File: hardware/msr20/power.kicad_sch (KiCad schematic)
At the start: 6 parts, among them U8 NCP1117-3.3_SOT223, U9 NCP1117-5.0_SOT223

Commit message: update footprint assignments for passives
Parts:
- C10, C11, C12, C13: footprint (none) -> Capacitor_SMD:C_0805_2012Metric
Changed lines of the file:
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@@
 			)
 		)
-		(property "Footprint" ""
+		(property "Footprint" "Capacitor_SMD:C_0805_2012Metric"
 			(at 152.0952 86.36 0)
 			(effects
@@
 			)
 		)
-		(property "Footprint" ""
+		(property "Footprint" "Capacitor_SMD:C_0805_2012Metric"
 			(at 181.3052 86.36 0)
 			(effects
@@
 			)
 		)
-		(property "Footprint" ""
+		(property "Footprint" "Capacitor_SMD:C_0805_2012Metric"
 			(at 105.1052 86.36 0)
 			(effects
@@
 			)
 		)
-		(property "Footprint" ""
+		(property "Footprint" "Capacitor_SMD:C_0805_2012Metric"
 			(at 74.6252 86.36 0)
 			(effects

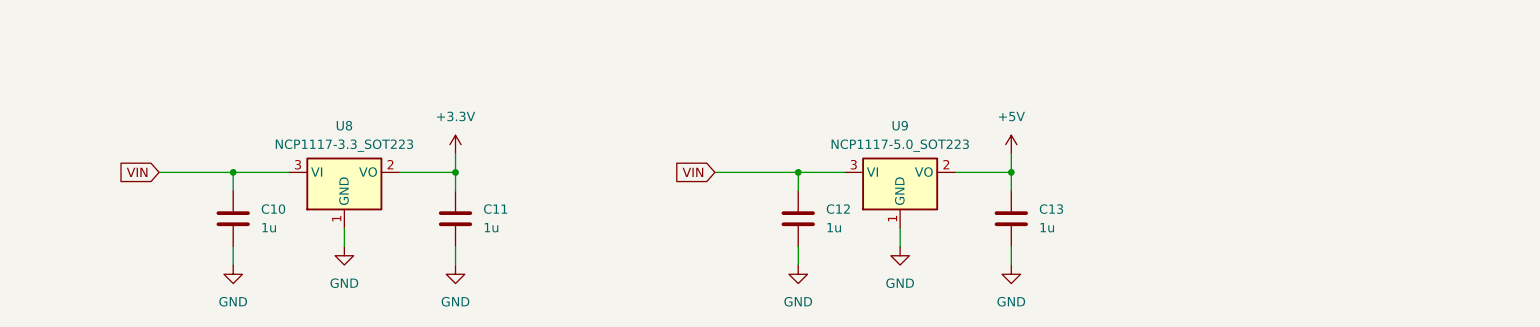
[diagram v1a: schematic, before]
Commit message: add 12v regulator
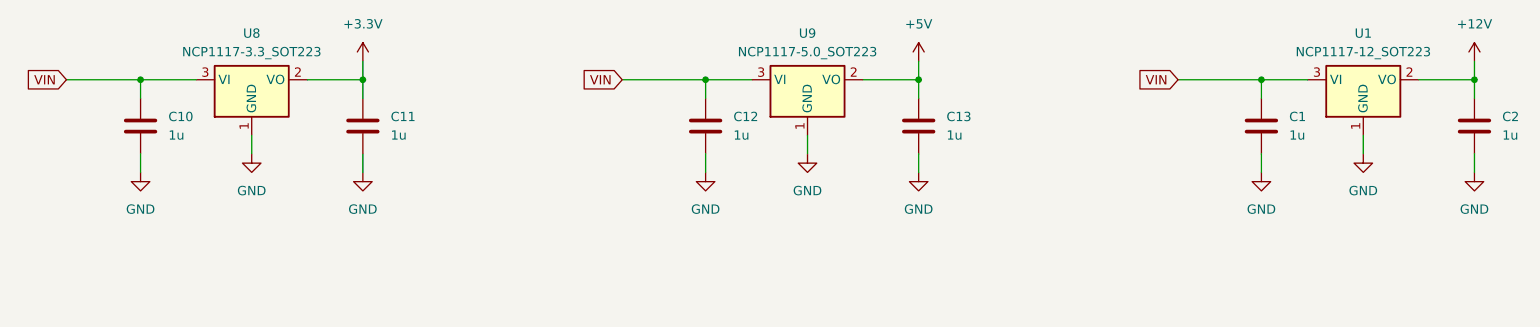
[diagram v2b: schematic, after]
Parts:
- added C1, C2: 1u, Capacitor_SMD:C_0805_2012Metric, symbol Device:C
- added U1: NCP1117-12_SOT223, Package_TO_SOT_SMD:SOT-223-3_TabPin2, symbol Regulator_Linear:NCP1117-12_SOT223
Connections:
- net GND: now also C1.2, C2.2, U1.1 (GND)
- net VIN: now also C1.1, U1.3 (VI)
- new net +12V: C2.1, U1.2 (VO)
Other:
- moved on the sheet: C10, C11, C12, C13, U8, U9
